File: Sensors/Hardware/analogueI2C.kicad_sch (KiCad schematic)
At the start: 57 parts, among them J1 Conn_01x03, J12 Conn_01x03, J13 Conn_01x03, J2 Conn_01x03, J3 Conn_01x03, J4 Conn_01x03, J5 Conn_01x03, J6 Conn_01x03, J7 Conn_01x03, J8 Conn_01x03, U13 ADS1219, U14 ADS1219, U15 ADS1219

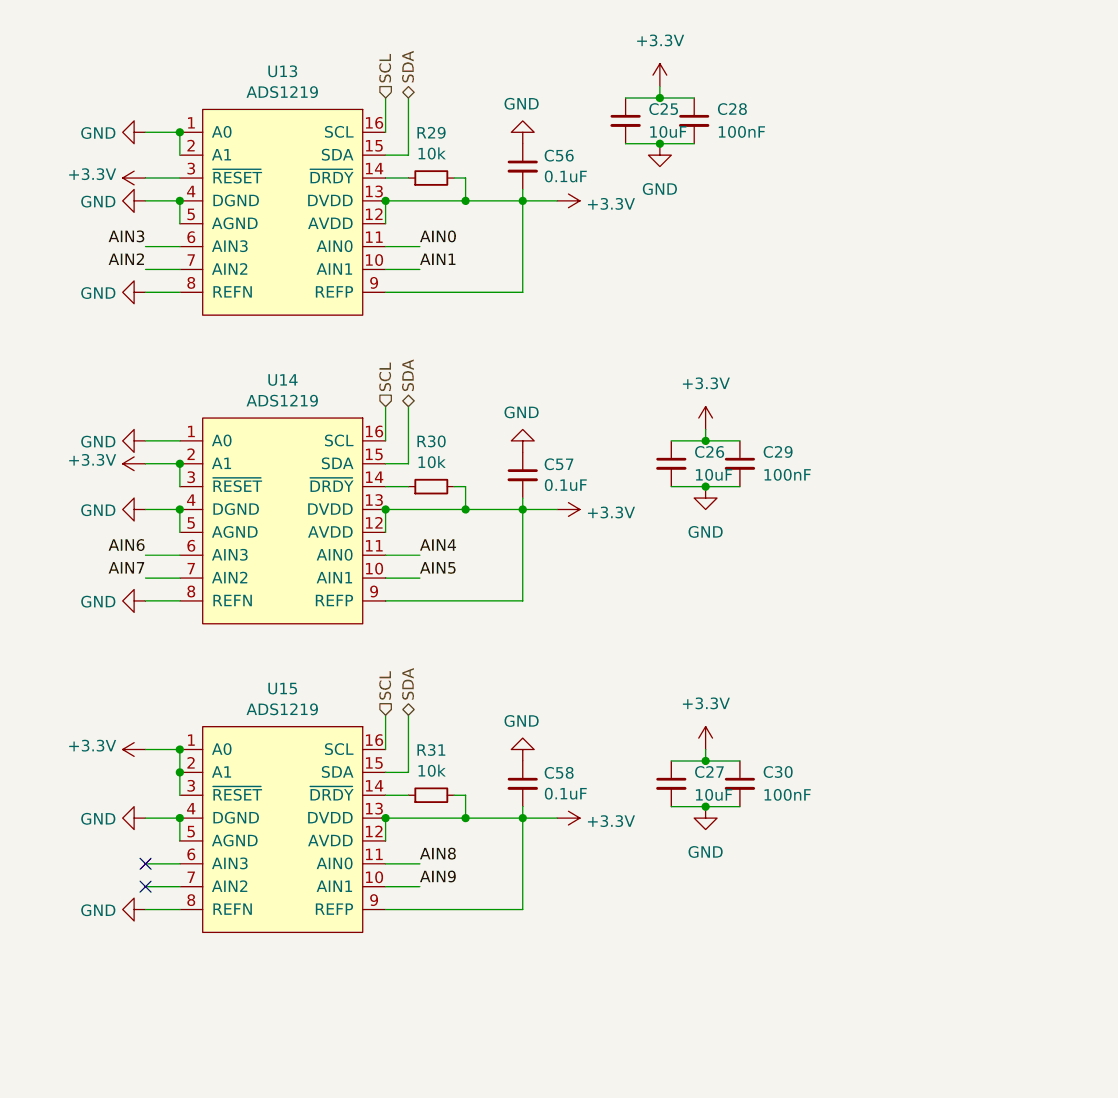
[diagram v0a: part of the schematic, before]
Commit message: added new ADC and some connections
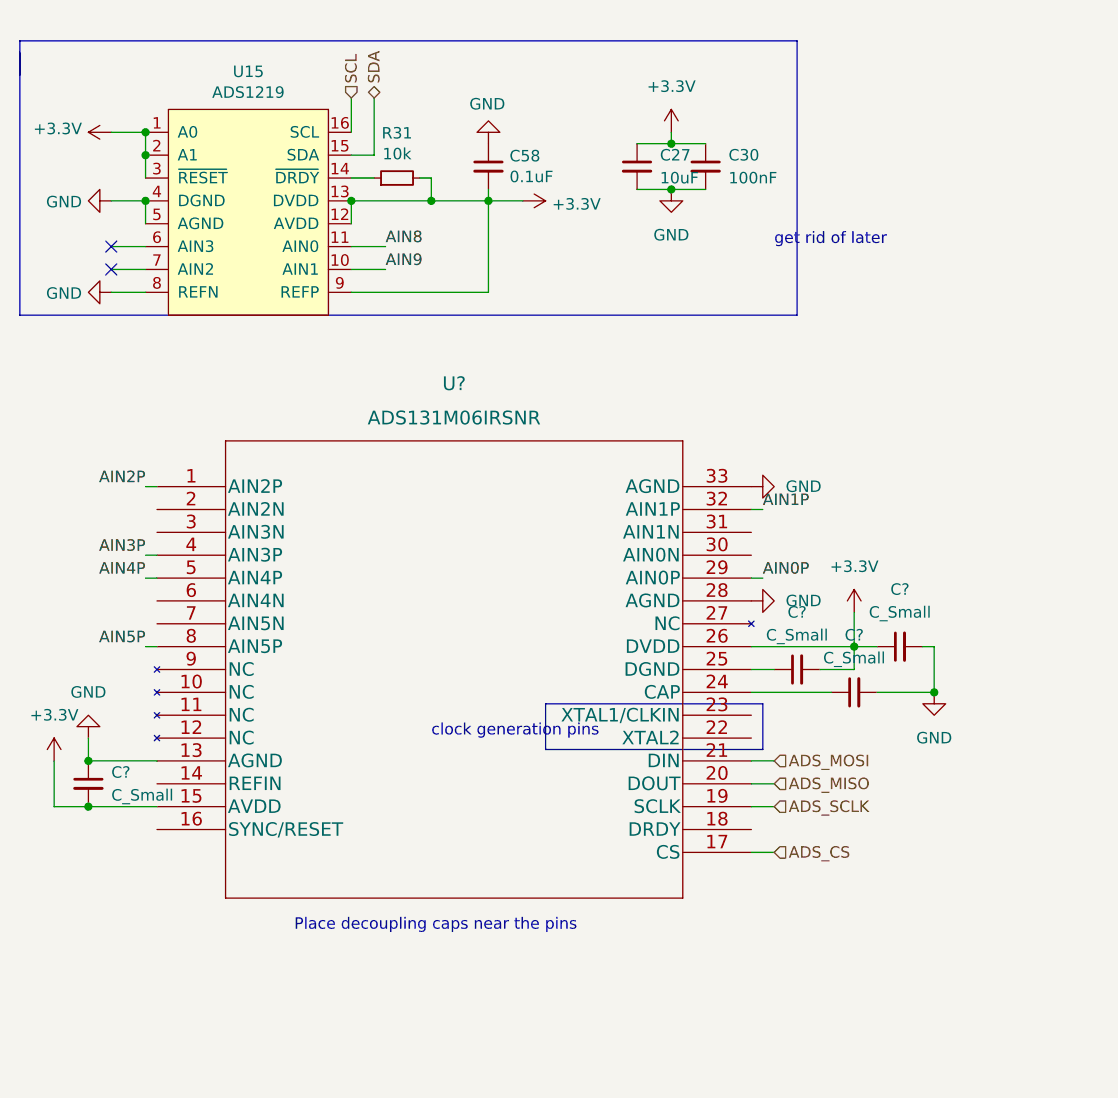
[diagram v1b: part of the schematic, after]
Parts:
- removed C25, C26: 10uF, Capacitor_SMD:C_0603_1608Metric, symbol Device:C_Small
- removed C28, C29: 100nF, Capacitor_SMD:C_0603_1608Metric, symbol Device:C_Small
- removed C56, C57: 0.1uF, Capacitor_SMD:C_0603_1608Metric, symbol Device:C_Small
- removed R29, R30: 10k, Resistor_SMD:R_0603_1608Metric, symbol Device:R_Small
- removed U13, U14: ADS1219, Package_SO:TSSOP-16_4.4x5mm_P0.65mm, symbol iclr:ADS1219
- added C? (x4): C_Small, symbol Device:C_Small
- added U?: ADS131M06IRSNR, QFN_M06IRSNR_TEX, symbol iclr:ADS131M06IRSNR
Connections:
- net +3V3: now also C?.1, C?.2, C?.2, U?.15 (AVDD), U?.26 (DVDD)
- net GND: now also C?.1, C?.2, C?.2, U?.13 (AGND), U?.28 (AGND), U?.33 (AGND)
- new net: C?.1, U?.25 (DGND)
- new net: C?.1, U?.24 (CAP)
- new net ADS_CS: U?.17 (CS)
- new net ADS_MISO: U?.20 (DOUT)
- new net ADS_MOSI: U?.21 (DIN)
- new net ADS_SCLK: U?.19 (SCLK)
- new net AIN0P: U?.29 (AIN0P)
- new net AIN1P: U?.32 (AIN1P)
- new net AIN2P: U?.1 (AIN2P)
- new net AIN3P: U?.4 (AIN3P)
- new net AIN4P: U?.5 (AIN4P)
- new net AIN5P: U?.8 (AIN5P)
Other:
- note added: "Place decoupling caps near the pins"
- note added: "clock generation pins"
- note added: "get rid of later"
- moved on the sheet: C27, C30, C58, R31, U15

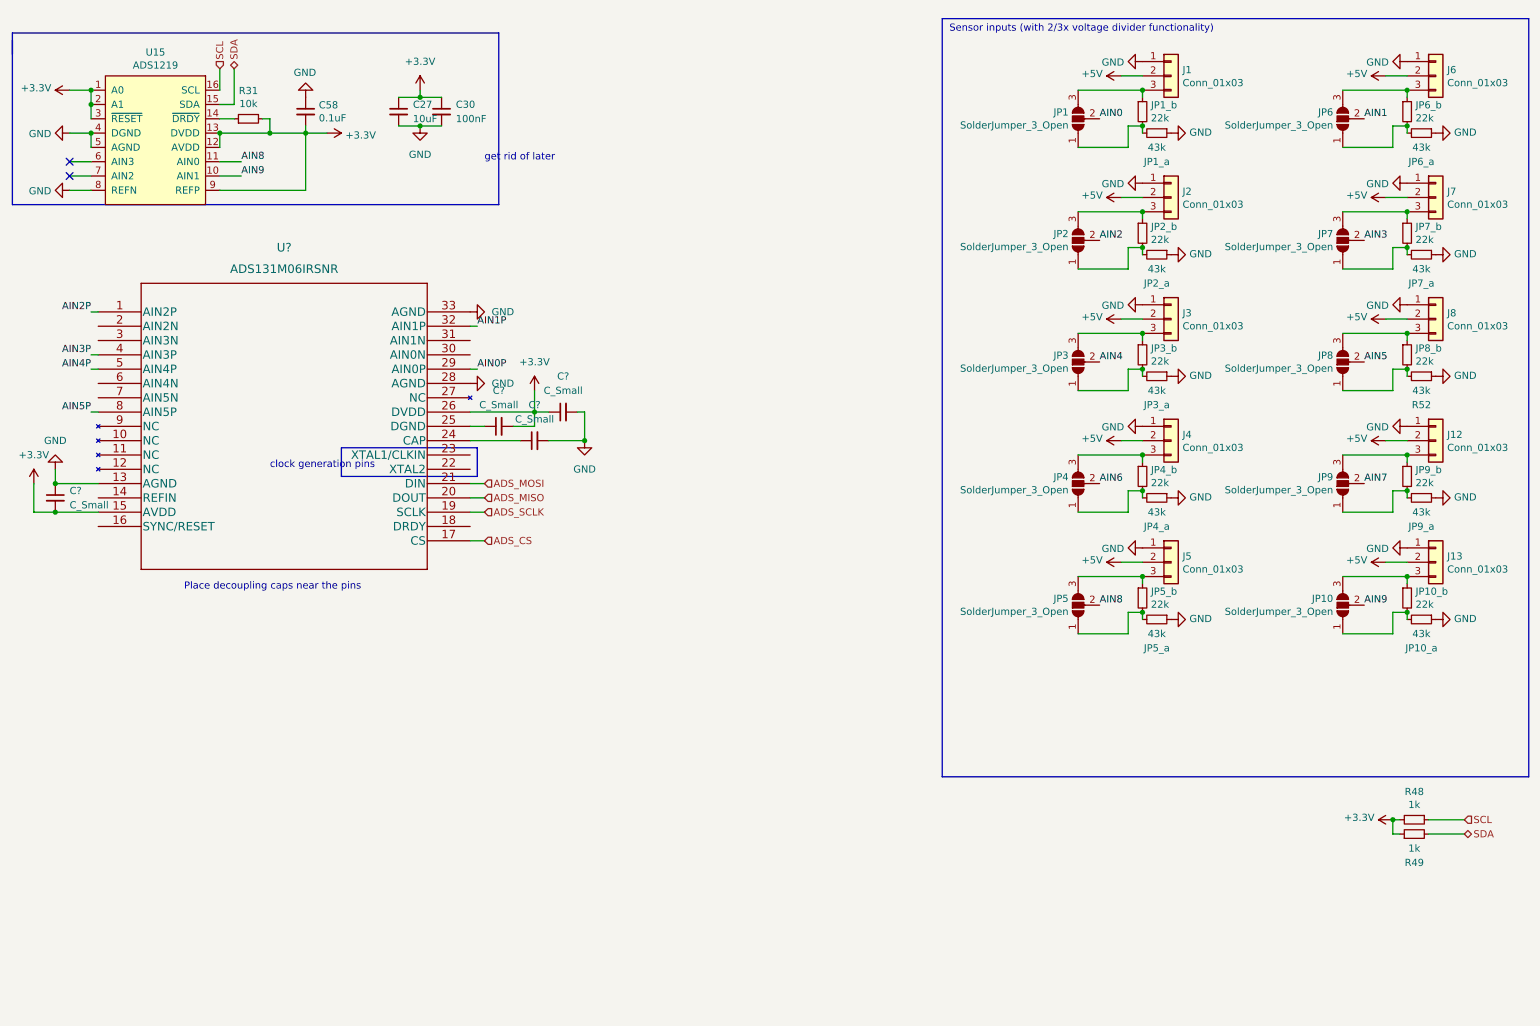
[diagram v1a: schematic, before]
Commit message: connectors and update
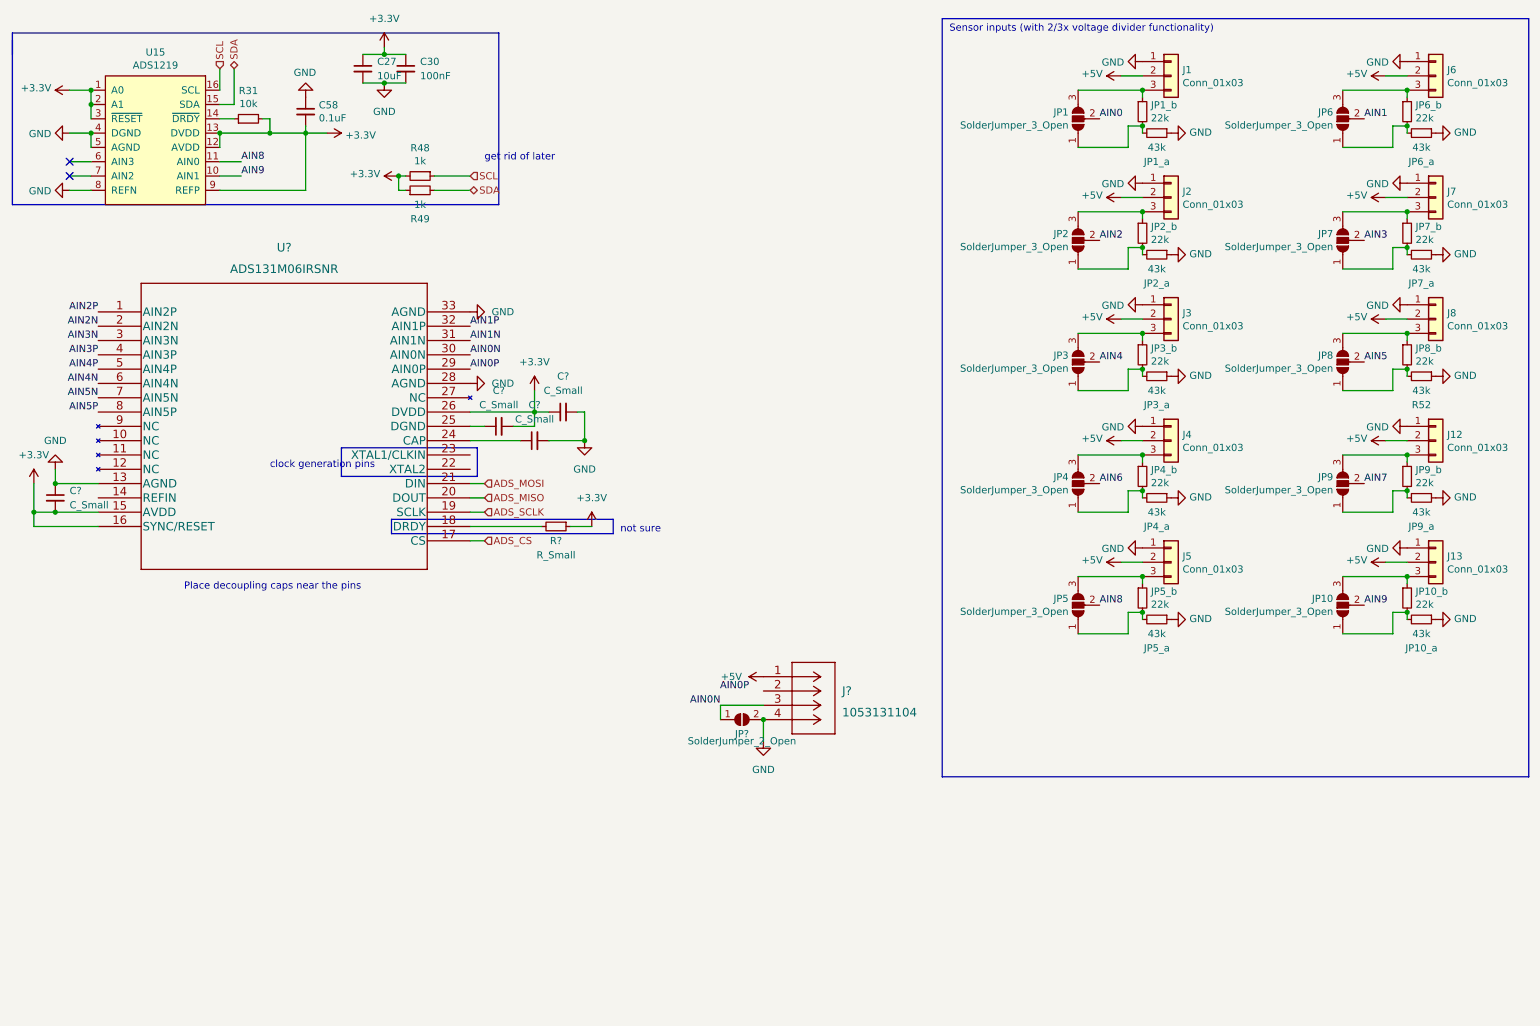
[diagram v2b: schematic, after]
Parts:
- added J?: 1053131104, CON_1053131104, symbol iclr:1053131104
- added JP?: SolderJumper_2_Open, symbol Jumper:SolderJumper_2_Open
- added R?: R_Small, symbol Device:R_Small
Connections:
- net +3V3: now also U?.16 (SYNC/RESET), R?.1
- net +5V: now also J?.1
- net GND: now also J?.4, JP?.2 (B)
- net at U?.18 (DRDY): now also R?.2
- net AIN2N: now reaches U?.2 (AIN2N)
- net AIN3N: now reaches U?.3 (AIN3N)
- net AIN0N: now reaches U?.30 (AIN0N)
- net AIN0N: now also J?.3, JP?.1 (A)
- net AIN1N: now reaches U?.31 (AIN1N)
- net AIN4N: now reaches U?.6 (AIN4N)
- net AIN5N: now reaches U?.7 (AIN5N)
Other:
- note added: "not sure"
- moved on the sheet: C27, C30, R48, R49

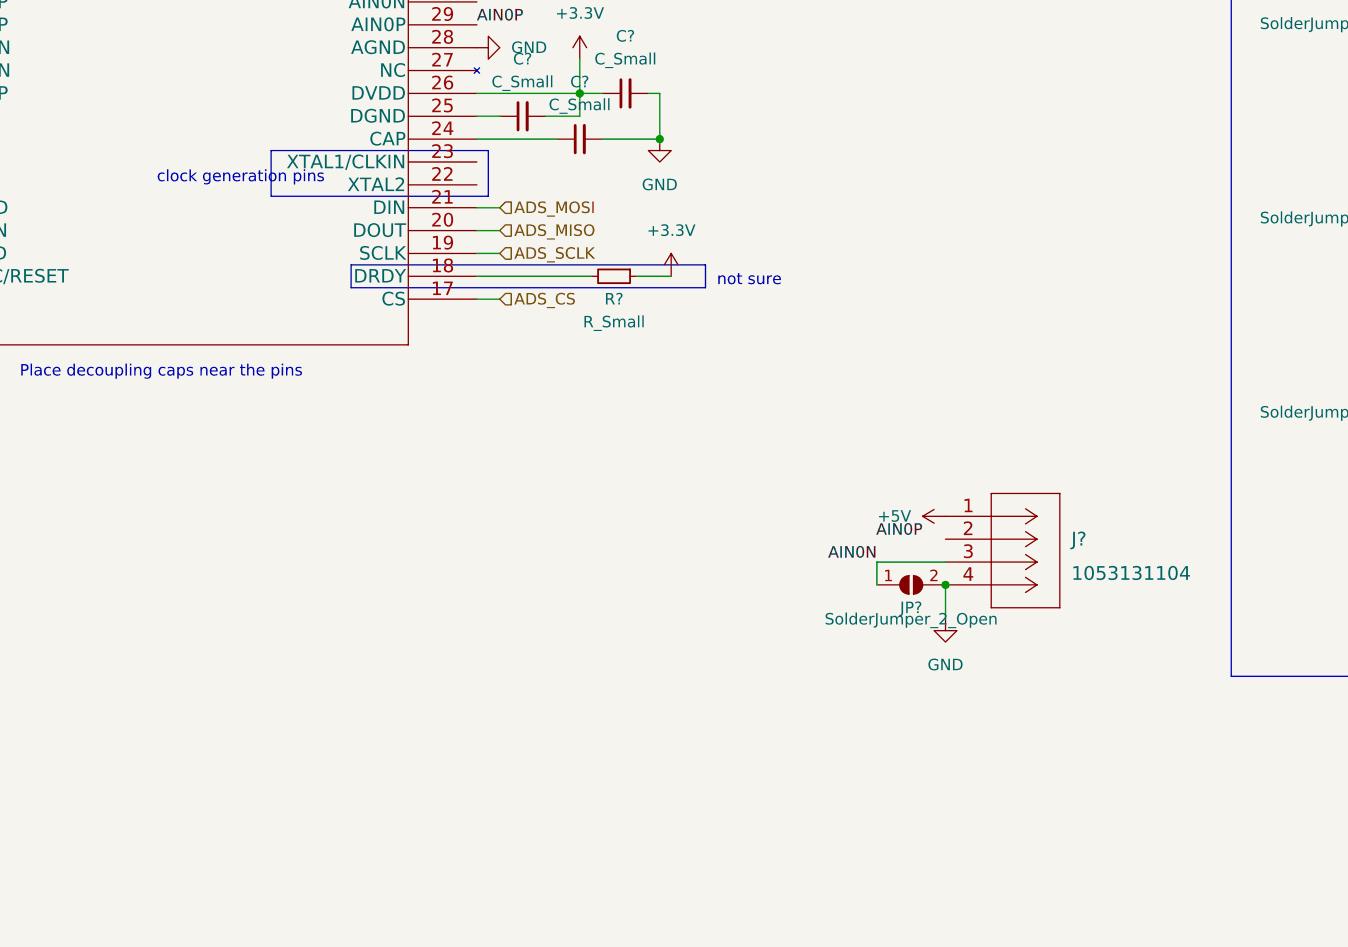
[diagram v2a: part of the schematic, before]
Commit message: potential divider preliminary
for connectors
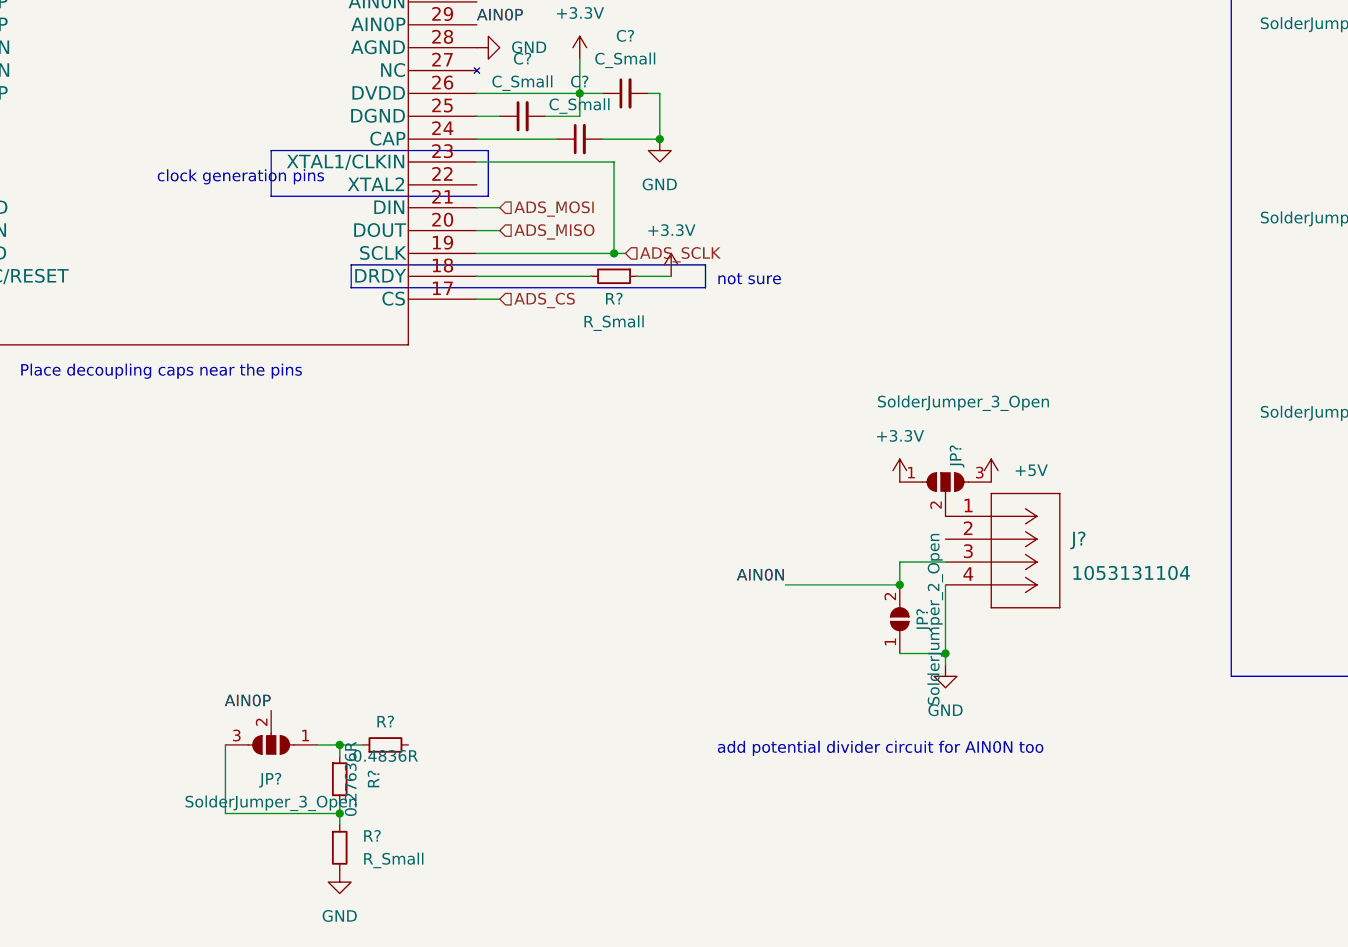
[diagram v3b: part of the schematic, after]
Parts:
- added JP?: SolderJumper_3_Open, Jumper:SolderJumper-3_P1.3mm_Open_RoundedPad1.0x1.5mm_NumberLabels, symbol Jumper:SolderJumper_3_Open
- added JP?: SolderJumper_3_Open, symbol Jumper:SolderJumper_3_Open
- added R?: 0.27636R, symbol Device:R_Small
- added R?: R_Small, symbol Device:R_Small
- added R?: 0.4836R, symbol Device:R_Small
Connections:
- net +3V3: now also JP?.1 (A)
- net +5V: now also JP?.3 (B); no longer J?.1
- net ADS_SCLK: now also U?.23 (XTAL1/CLKIN)
- net AIN0N: now also JP?.2 (B); no longer JP?.1 (A)
- net AIN0P: now also JP?.2 (C)
- net GND: now also JP?.1 (A), R?.2; no longer JP?.2 (B)
- new net: J?.1, JP?.2 (C)
- new net: JP?.1 (A), R?.1, R?.1
- new net: JP?.3 (B), R?.1, R?.2
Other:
- note added: "add potential divider circuit for AIN0N too"
- moved on the sheet: JP?
